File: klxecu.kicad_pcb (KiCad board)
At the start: 2 copper layers, 91 parts, among them IC1 SP721, J1 Conn_02x18_Top_Bottom, J2 ICSP, J3 Arduino Comms Header, Q1 STP62NS04Z, Q2 STP62NS04Z, Q3 IRF7301PBF, Q4 STP62NS04Z, U1 ATmega2560-16A, U2 MAX9924UAUB+, U3 ERZ-V14D220, U4 LM340T-5.0, U5 74LS02DR, U6 74LS14DR, U7 TC4422AVPA, Y1 16 mhz

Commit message: Updates
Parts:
- removed C25: u1, Capacitor_THT:C_Disc_D3.8mm_W2.6mm_P2.50mm
- removed C26: 47uf, Capacitor_THT:CP_Radial_Tantal_D6.0mm_P2.50mm
- removed C27: 1uf, Capacitor_SMD:C_0805_2012Metric_Pad1.18x1.45mm_HandSolder
- removed D2, D5, D7: 1N4004, Diode_THT:D_DO-41_SOD81_P10.16mm_Horizontal
- removed D6: 1N5919BG, Diode_THT:D_DO-41_SOD81_P7.62mm_Horizontal
- removed LED3, LED4: GREEN, LED_SMD:LED_0805_2012Metric_Pad1.15x1.40mm_HandSolder
- removed R34: 2k, Resistor_SMD:R_0805_2012Metric_Pad1.20x1.40mm_HandSolder
- removed R35: 47 2w, Resistor_THT:R_Axial_DIN0207_L6.3mm_D2.5mm_P5.08mm_Vertical
- removed U7: TC4422AVPA, Package_DIP:DIP-8_W7.62mm
- removed Y1: 16 mhz, Crystal:Resonator_SMD_Murata_CSTxExxV-3Pin_3.0x1.1mm_HandSoldering
- added A1: Pololu_Breakout_A4988, Module:Pololu_Breakout-16_15.2x20.3mm, F.Cu at (88.3, 146.1)
- added Q5: STP62NS04Z, Package_TO_SOT_THT:TO-220-3_Vertical, F.Cu at (153.0, 114.0)
- C10: value 1nf -> 0.1uf
- C12, C17: value 0.22uF -> 0.1uf
- C13: moved to B.Cu
- C14, C5, C7: value 0.1uf -> 0.22uF; moved to B.Cu
- C15: value 0.1uf -> 0.33uF; moved to B.Cu
- C16: value 0.1uf -> 10nf
- C18: value 0.22uF -> 1uf
- C19: value 0.33uF -> 100uf; footprint Capacitor_SMD:C_0805_2012Metric_Pad1.18x1.45mm_HandSolder -> Capacitor_THT:CP_Radial_D5.0mm_P2.50mm
- C2: value 0.1uf -> 1nf
- C20: value 10nf -> 1uf
- C21: value 0.1uf -> 10uf; footprint Capacitor_SMD:C_0805_2012Metric_Pad1.18x1.45mm_HandSolder -> Capacitor_THT:CP_Radial_Tantal_D6.0mm_P2.50mm
- C22: value 1uf -> u1; footprint Capacitor_SMD:C_0805_2012Metric_Pad1.18x1.45mm_HandSolder -> Capacitor_THT:C_Disc_D3.8mm_W2.6mm_P2.50mm
- C23: value 10uf -> u1; footprint Capacitor_THT:CP_Radial_Tantal_D6.0mm_P2.50mm -> Capacitor_THT:C_Disc_D3.8mm_W2.6mm_P2.50mm
- C24: value u1 -> 47uf; footprint Capacitor_THT:C_Disc_D3.8mm_W2.6mm_P2.50mm -> Capacitor_THT:CP_Radial_Tantal_D6.0mm_P2.50mm
- C4: value 22pf -> 0.1uf
- C6: value 0.1uf -> 0.22uF
- D1: value 1N5818 -> 1N4004; footprint Diode_THT:D_DO-41_SOD81_P7.62mm_Horizontal -> Diode_THT:D_DO-41_SOD81_P10.16mm_Horizontal
- D3: value 1N4004 -> 1N5818; footprint Diode_THT:D_DO-41_SOD81_P10.16mm_Horizontal -> Diode_THT:D_DO-41_SOD81_P7.62mm_Horizontal
- D4: value 1N4004 -> 1N5919BG; footprint Diode_THT:D_DO-41_SOD81_P10.16mm_Horizontal -> Diode_THT:D_DO-41_SOD81_P7.62mm_Horizontal
- J1: value Conn_02x18_Top_Bottom -> Conn_02x20_Odd_Even; footprint Connector_PinHeader_2.54mm:PinHeader_2x18_P2.54mm_Vertical -> Connector_PinSocket_2.54mm:PinSocket_2x20_P2.54mm_Vertical
- J2: value ICSP -> Conn_02x18_Top_Bottom; footprint Connector_PinHeader_2.54mm:PinHeader_2x03_P2.54mm_Vertical -> Connector_PinHeader_2.54mm:PinHeader_2x18_P2.54mm_Vertical
- J3: value Arduino Comms Header -> Conn_02x16_Odd_Even; footprint Connector_PinHeader_2.54mm:PinHeader_1x06_P2.54mm_Vertical -> Connector_PinSocket_2.54mm:PinSocket_2x16_P2.54mm_Vertical
- JP2: value Jumper_2_Open -> Jumper_3_Open; footprint Connector_PinHeader_2.54mm:PinHeader_1x02_P2.54mm_Vertical -> Connector_PinHeader_2.54mm:PinHeader_1x03_P2.54mm_Vertical
- Q3: value IRF7301PBF -> STP62NS04Z; footprint Package_SO:SOIC-8_3.9x4.9mm_P1.27mm -> Package_TO_SOT_THT:TO-220-3_Vertical
- R1: value 1M -> 10k; footprint Resistor_SMD:R_0805_2012Metric_Pad1.20x1.40mm_HandSolder -> Resistor_THT:R_Axial_DIN0207_L6.3mm_D2.5mm_P5.08mm_Vertical
- R10, R13, R14, R15, R9: value 470k -> 470; footprint Resistor_SMD:R_0805_2012Metric_Pad1.20x1.40mm_HandSolder -> Resistor_THT:R_Axial_DIN0207_L6.3mm_D2.5mm_P5.08mm_Vertical
- R11, R12, R16, R17, R19, R21, R25, R28: footprint Resistor_SMD:R_0805_2012Metric_Pad1.20x1.40mm_HandSolder -> Resistor_THT:R_Axial_DIN0207_L6.3mm_D2.5mm_P5.08mm_Vertical
- R18, R29: value 2k -> 100k; footprint Resistor_SMD:R_0805_2012Metric_Pad1.20x1.40mm_HandSolder -> Resistor_THT:R_Axial_DIN0207_L6.3mm_D2.5mm_P5.08mm_Vertical
- R2: value 10k -> 4.7k; footprint Resistor_SMD:R_0805_2012Metric_Pad1.20x1.40mm_HandSolder -> Resistor_THT:R_Axial_DIN0207_L6.3mm_D2.5mm_P5.08mm_Vertical
- R20, R30, R31: value 100k -> 1k; footprint Resistor_SMD:R_0805_2012Metric_Pad1.20x1.40mm_HandSolder -> Resistor_THT:R_Axial_DIN0207_L6.3mm_D2.5mm_P5.08mm_Vertical
- R22: value 1k -> 100k; footprint Resistor_SMD:R_0805_2012Metric_Pad1.20x1.40mm_HandSolder -> Resistor_THT:R_Axial_DIN0207_L6.3mm_D2.5mm_P5.08mm_Vertical
- R23, R24: value 10k -> 1k; footprint Resistor_SMD:R_0805_2012Metric_Pad1.20x1.40mm_HandSolder -> Resistor_THT:R_Axial_DIN0207_L6.3mm_D2.5mm_P5.08mm_Vertical
- R26, R27: value 1k -> 10k; footprint Resistor_SMD:R_0805_2012Metric_Pad1.20x1.40mm_HandSolder -> Resistor_THT:R_Axial_DIN0207_L6.3mm_D2.5mm_P5.08mm_Vertical
- R3: value 4.7k -> 2.49k; footprint Resistor_SMD:R_0805_2012Metric_Pad1.20x1.40mm_HandSolder -> Resistor_THT:R_Axial_DIN0207_L6.3mm_D2.5mm_P5.08mm_Vertical
- R32: value 1k -> 2k; footprint Resistor_SMD:R_0805_2012Metric_Pad1.20x1.40mm_HandSolder -> Resistor_THT:R_Axial_DIN0207_L6.3mm_D2.5mm_P5.08mm_Vertical
- R33: value 1k -> 47 2w; footprint Resistor_SMD:R_0805_2012Metric_Pad1.20x1.40mm_HandSolder -> Resistor_THT:R_Axial_DIN0207_L6.3mm_D2.5mm_P5.08mm_Vertical
- R4, R5: value 2.49k -> 10k; footprint Resistor_SMD:R_0805_2012Metric_Pad1.20x1.40mm_HandSolder -> Resistor_THT:R_Axial_DIN0207_L6.3mm_D2.5mm_P5.08mm_Vertical
- R6: value 10k -> 2.49k; footprint Resistor_SMD:R_0805_2012Metric_Pad1.20x1.40mm_HandSolder -> Resistor_THT:R_Axial_DIN0207_L6.3mm_D2.5mm_P5.08mm_Vertical
- R7: value 10k -> 470k; footprint Resistor_SMD:R_0805_2012Metric_Pad1.20x1.40mm_HandSolder -> Resistor_THT:R_Axial_DIN0207_L6.3mm_D2.5mm_P5.08mm_Vertical
- R8: value 470k -> 470
- U1: value ATmega2560-16A -> MAX9924UAUB+; footprint Package_QFP:TQFP-100_14x14mm_P0.5mm -> Package_SO:MSOP-10_3x3mm_P0.5mm
- U2: value MAX9924UAUB+ -> ATtiny84-20P; footprint Package_SO:MSOP-10_3x3mm_P0.5mm -> Package_DIP:DIP-14_W7.62mm
- U3: value ERZ-V14D220 -> 74LS14DR; footprint Varistor:RV_Disc_D7mm_W3.4mm_P5mm -> Package_SO:SOIC-14_3.9x8.7mm_P1.27mm
- U4: value LM340T-5.0 -> TC4422AVPA; footprint Package_TO_SOT_THT:TO-220-3_Vertical -> Package_DIP:DIP-8_W7.62mm
- U5: value 74LS02DR -> ERZ-V14D220; footprint Package_SO:SOIC-14_3.9x8.7mm_P1.27mm -> Varistor:RV_Disc_D7mm_W3.4mm_P5mm
- U6: value 74LS14DR -> LM340T-5.0; footprint Package_SO:SOIC-14_3.9x8.7mm_P1.27mm -> Package_TO_SOT_THT:TO-220-3_Vertical
- moved U6 201.0 mm to (245.1, 35.6), turned to -90 degrees
- moved U5 191.1 mm to (247.0, 25.4), turned to -90 degrees
- moved J2 186.8 mm to (25.4, 20.3)
- moved R26 184.4 mm to (51.0, 21.6)
- moved R1 184.4 mm to (33.7, 36.0), turned to 90 degrees
- moved R27 178.0 mm to (58.0, 24.1)
- moved JP1 172.6 mm to (33.7, 40.0)
- moved C22 168.3 mm to (229.2, 25.4), turned to -90 degrees
- moved R8 168.0 mm to (141.6, 17.1), turned to -90 degrees
- moved C13 162.6 mm to (134.6, 21.6), turned to 90 degrees
- moved R25 158.3 mm to (33.9, 117.5)
- moved R33 154.1 mm to (19.3, 114.9)
- moved R32 152.7 mm to (33.9, 125.7)
- moved R12 152.3 mm to (30.1, 184.2)
- moved C7 150.6 mm to (137.2, 31.8), turned to -90 degrees
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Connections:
- C1 pad 1: +5V -> TPS
- C10 pad 2: Net-(C10-Pad2) -> GND
- C11 pad 1: ARDUINO-A3 -> ATTINY-A1
- C12 pad 1: ARDUINO-A4 -> MAP
- C13 pad 1: ARDUINO-A5 -> ARDUINO-A2
- C14 pad 1: O2S + -> ARDUINO-A1
- C15 pad 1: Net-(C15-Pad1) -> ARDUINO-A0
- C16 pad 1: MAP -> +5V
- C17 pad 1: ARDUINO-A2 -> +5V
- C18 pad 1: ARDUINO-A1 -> +5V
- C19 pad 1: ARDUINO-A0 -> +BATT
- C2 pad 1: +5V -> Net-(C2-Pad1)
- C2 pad 2: GND -> Net-(C2-Pad2)
- C21 pad 1: +5V -> +12V
- C22 pad 1: +5V -> +12V
- C23 pad 1: +12V -> +5V
- C24 pad 1: +12V -> +5V
- C3 pad 1: +5V -> CLT
- C4 pad 1: ARDUINO-RST -> IAT
- C5 pad 1: Net-(C5-Pad1) -> ARDUINO-A3
- C6 pad 1: Net-(C6-Pad1) -> ARDUINO-A4
- C6 pad 2: ARDUINO-RST -> GND
- C7 pad 1: TPS -> ARDUINO-A5
- C8 pad 1: CLT -> SUB TPS
- C9 pad 1: IAT -> O2S +
- D1 pad 1: Net-(D1-Pad1) -> INJECTOR
- D1 pad 2: +12V -> Net-(D1-Pad2)
- D3 pad 1: FP RELAY -> Net-(D3-Pad1)
- D3 pad 2: Net-(D3-Pad2) -> +12V
- D4 pad 1: Net-(D4-Pad1) -> +5V
- D4 pad 2: ARDUINO-D6 -> GND
- IC1 pad 4: Earth -> GND
- J1 pad 1: +BATT -> unconnected-(J1-Pad1)
- J1 pad 10: TEMP WARN -> unconnected-(J1-Pad10)
- J1 pad 11: KICKSTAND SW -> unconnected-(J1-Pad11)
- J1 pad 12: AIR VALVE -> unconnected-(J1-Pad12)
- J1 pad 13: SUB A - -> ARDUINO-D4
- J1 pad 14: SUB B - -> ARDUINO-D5
- J1 pad 15: FAN RELAY -> ARDUINO-D6
- J1 pad 16: KILL SW -> ARDUINO-D7
- J1 pad 17: GND -> ARDUINO-D8
- J1 pad 18: GND -> ARDUINO-D8
- J1 pad 19: +12V -> unconnected-(J1-Pad19)
- J1 pad 2: NEUTRAL SW -> unconnected-(J1-Pad2)
- J1 pad 20: Vehicle Down -> unconnected-(J1-Pad20)
- J1 pad 21: CKP + -> unconnected-(J1-Pad21)
- J1 pad 23: TPS -> unconnected-(J1-Pad23)
- J1 pad 24: MAP -> unconnected-(J1-Pad24)
- J1 pad 25: O2S + -> unconnected-(J1-Pad25)
- J1 pad 26: GND -> unconnected-(J1-Pad26)
- J1 pad 27: CKP - -> unconnected-(J1-Pad27)
- J1 pad 28: GND -> ARDUINO-D19
- J1 pad 29: FP RELAY -> unconnected-(J1-Pad29)
- J1 pad 3: CHECK ENGINE -> GND
- J1 pad 30: CLUTCH SW -> unconnected-(J1-Pad30)
- J1 pad 31: +5V -> unconnected-(J1-Pad31)
- J1 pad 32: SUB B + -> ARDUINO-D23
- J1 pad 33: SUB A + -> unconnected-(J1-Pad33)
- J1 pad 34: INJECTOR -> unconnected-(J1-Pad34)
- J1 pad 35: O2S HEAT + -> unconnected-(J1-Pad35)
- J1 pad 36: IGN -> unconnected-(J1-Pad36)
- J1 pad 4: CLT -> GND
- J1 pad 5: ARDUINO-D3 -> +5V
- J1 pad 6: GND -> +5V
- J1 pad 7: IAT -> unconnected-(J1-Pad7)
- J1 pad 8: SPEED -> ARDUINO-RST
- J1 pad 9: SUB TPS -> unconnected-(J1-Pad9)
- J2 pad 1: Net-(J2-Pad1) -> +BATT
- J2 pad 2: +5V -> NEUTRAL SW
- J2 pad 3: Net-(J2-Pad3) -> CHECK ENGINE
- J2 pad 4: Net-(J2-Pad4) -> CLT
- J2 pad 5: ARDUINO-RST -> ARDUINO-D3
- J3 pad 1: GND -> ARDUINO-A0
- J3 pad 2: GND -> ARDUINO-A1
- J3 pad 3: +5V -> ARDUINO-A2
- J3 pad 4: Net-(J3-Pad4) -> ARDUINO-A3
- J3 pad 5: Net-(J3-Pad5) -> ARDUINO-A4
- J3 pad 6: Net-(C6-Pad1) -> ARDUINO-A5
- JP2 pad 1: Net-(D5-Pad1) -> +5V
- JP2 pad 2: Net-(D4-Pad1) -> Net-(A1-Pad8)
- LED1 pad 1: Net-(D2-Pad2) -> Net-(D1-Pad2)
- LED2 pad 1: Net-(D3-Pad2) -> GND
- Q3 pad 1: GND -> Net-(Q3-Pad1)
- Q3 pad 2: Net-(Q3-Pad2) -> CHECK ENGINE
- Q4 pad 2: FAN RELAY -> TEMP WARN
- R1 pad 1: Net-(R1-Pad1) -> +5V
- R1 pad 2: Net-(R1-Pad2) -> ARDUINO-D3
- R10 pad 1: IAT -> SUB TPS
- R10 pad 2: ARDUINO-A5 -> ATTINY-A1
- R11 pad 1: Net-(C15-Pad1) -> Net-(C10-Pad1)
- R12 pad 2: Net-(C15-Pad1) -> Net-(C10-Pad1)
- R14 pad 1: Net-(C15-Pad1) -> Net-(C10-Pad1)
- R18 pad 1: KILL SW -> ARDUINO-D8
- R18 pad 2: Net-(LED2-Pad2) -> GND
- R19 pad 1: ARDUINO-D8 -> ARDUINO-D4
- R2 pad 1: +5V -> CKP+
- R2 pad 2: ARDUINO-D3 -> CKP-
- R20 pad 1: ARDUINO-D4 -> Net-(Q1-Pad1)
- R20 pad 2: GND -> ARDUINO-D8
- R21 pad 1: Net-(Q1-Pad1) -> Net-(Q2-Pad1)
- R21 pad 2: ARDUINO-D8 -> ARDUINO-D4
- R22 pad 1: Net-(Q2-Pad1) -> ATTINY-D10
- R22 pad 2: ARDUINO-D4 -> GND
- R23 pad 1: +5V -> Net-(Q3-Pad1)
- R23 pad 2: NEUTRAL SW -> ATTINY-D10
- R24 pad 1: +5V -> ARDUINO-D23
- R24 pad 2: KICKSTAND SW -> Net-(R24-Pad2)
- R25 pad 1: Net-(D4-Pad1) -> Net-(R24-Pad2)
- R26 pad 1: Net-(Q3-Pad4) -> +5V
- R26 pad 2: Net-(D4-Pad1) -> NEUTRAL SW
- R27 pad 1: ARDUINO-D23 -> +5V
- R27 pad 2: Net-(R27-Pad2) -> KICKSTAND SW
- R28 pad 1: Net-(R27-Pad2) -> ARDUINO-D5
- R29 pad 1: +12V -> ARDUINO-D7
- R29 pad 2: Net-(LED3-Pad2) -> GND
- R3 pad 1: CKP+ -> +5V
- R3 pad 2: CKP- -> CLT
- R30 pad 1: ARDUINO-D5 -> Net-(Q5-Pad1)
- R30 pad 2: GND -> ARDUINO-D5
- R31 pad 1: ARDUINO-D7 -> Net-(Q4-Pad1)
- R31 pad 2: GND -> ARDUINO-D7
- R32 pad 1: Net-(Q4-Pad1) -> Net-(R32-Pad1)
- R32 pad 2: ARDUINO-D5 -> Net-(LED2-Pad2)
- R33 pad 1: Net-(Q3-Pad2) -> IGN
- R33 pad 2: ARDUINO-D7 -> Net-(R32-Pad1)
- R4 pad 1: +5V -> Net-(C2-Pad1)
- R4 pad 2: CLT -> CKP+
- R5 pad 1: +5V -> CKP-
- R5 pad 2: IAT -> Net-(C2-Pad2)
- R6 pad 1: Net-(C10-Pad1) -> +5V
- R6 pad 2: CKP+ -> IAT
- R7 pad 1: CKP- -> TPS
- R7 pad 2: Net-(C10-Pad2) -> ARDUINO-A3
- R8 pad 1: TPS -> CLT
- R8 pad 2: ARDUINO-A3 -> ARDUINO-A4
- R9 pad 1: CLT -> IAT
- R9 pad 2: ARDUINO-A4 -> ARDUINO-A5
- U1 pad 1: ARDUINO-D4 -> Net-(C2-Pad1)
- U1 pad 2: Net-(J3-Pad4) -> Net-(C2-Pad2)
- U1 pad 3: Net-(J3-Pad5) -> unconnected-(U1-Pad3)
- U1 pad 4: unconnected-(U1-Pad4) -> GND
- U1 pad 5: ARDUINO-D5 -> GND
- U1 pad 6: unconnected-(U1-Pad6) -> GND
- U1 pad 7: ARDUINO-D3 -> ARDUINO-D19
- U1 pad 9: unconnected-(U1-Pad9) -> GND
- U2 pad 1: Net-(C10-Pad1) -> +5V
- U2 pad 10: +5V -> ATTINY-A3
- U2 pad 2: Net-(C10-Pad2) -> ATTINY-D10
- U2 pad 3: unconnected-(U2-Pad3) -> ARDUINO-RST
- U2 pad 4: GND -> +5V
- U2 pad 5: GND -> ARDUINO-D6
- U2 pad 6: GND -> unconnected-(U2-Pad6)
- U2 pad 7: ARDUINO-D19 -> Net-(A1-Pad16)
- U2 pad 8: unconnected-(U2-Pad8) -> Net-(A1-Pad15)
- U2 pad 9: GND -> ATTINY-A4
- U3 pad 1: +12V -> Vehicle Down
- U3 pad 2: GND -> ATTINY-A2
- U4 pad 1: Net-(D1-Pad1) -> +5V
- U4 pad 2: GND -> Net-(R24-Pad2)
- U4 pad 3: +5V -> unconnected-(U4-Pad3)
- U5 pad 1: ARDUINO-RST -> +12V
- U5 pad 2: Net-(U5-Pad2) -> GND
- U6 pad 1: Vehicle Down -> Net-(D3-Pad1)
- U6 pad 2: Net-(U5-Pad2) -> GND
- U6 pad 3: NEUTRAL SW -> +5V
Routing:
- net +12V: track 95.2 -> 29.5 mm
- net Net-(D1-Pad1): track 16.0 -> 0.00 mm
- net ARDUINO-RST: track 14.5 -> 0.00 mm
- net Net-(U5-Pad2): track 12.0 -> 0.00 mm
- net Net-(U5-Pad5): track 12.0 -> 0.00 mm
- net Net-(U5-Pad6): track 11.9 -> 0.00 mm
- net KICKSTAND SW: track 9.65 -> 0.00 mm
- net ARDUINO-D19: track 0.00 -> 9.41 mm
- net GND: track 58.5 -> 67.0 mm
- net Net-(U5-Pad11): track 7.95 -> 0.00 mm
- net Net-(C2-Pad1): track 0.00 -> 6.28 mm
- net Net-(C2-Pad2): track 0.00 -> 5.67 mm
- net Net-(U5-Pad13): track 5.48 -> 0.00 mm
- net Net-(D3-Pad1): track 0.00 -> 5.10 mm
- net NEUTRAL SW: track 4.79 -> 0.00 mm
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
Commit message: more updates
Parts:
- C13, C14, C15, C5, C7: moved to F.Cu
- R1, R10, R11, R12, R13, R14, R15, R16, R17, R18, R19, R2, R20, R21, R22, R23, R24, R25, R26, R27, R28, R29, R3, R30, R31, R32, R6, R9: footprint Resistor_THT:R_Axial_DIN0207_L6.3mm_D2.5mm_P5.08mm_Vertical -> Resistor_SMD:R_0805_2012Metric_Pad1.20x1.40mm_HandSolder
- R4, R5: footprint Resistor_THT:R_Axial_DIN0207_L6.3mm_D2.5mm_P5.08mm_Vertical -> Resistor_SMD:R_0805_2012Metric
- R7: value 470k -> 470; footprint Resistor_THT:R_Axial_DIN0207_L6.3mm_D2.5mm_P5.08mm_Vertical -> Resistor_SMD:R_0805_2012Metric_Pad1.20x1.40mm_HandSolder
- moved C8 182.8 mm to (88.9, 142.7)
- moved R10 180.6 mm to (85.1, 141.5), turned to 90 degrees
- moved C11 177.3 mm to (88.9, 140.2)
- moved R9 174.3 mm to (118.2, 32.0), turned to 90 degrees
- moved R12 168.8 mm to (104.0, 32.4), turned to 90 degrees
- moved C4 168.2 mm to (121.4, 33.9)
- moved R13 165.3 mm to (111.7, 21.5), turned to -90 degrees
- moved R6 163.8 mm to (121.4, 36.5), turned to 180 degrees
- moved C9 163.0 mm to (114.8, 20.0)
- moved R11 162.9 mm to (102.8, 29.5), turned to 180 degrees
- moved C10 162.5 mm to (106.6, 32.4), turned to -90 degrees
- moved R14 155.8 mm to (107.2, 29.5)
- moved U1 106.8 mm to (129.2, 54.5)
- moved C16 106.5 mm to (139.0, 54.5)
- moved C17 106.5 mm to (136.4, 54.5)
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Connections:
- A1 pad 8: Net-(A1-Pad8) -> Net-(C19-Pad1)
- C19 pad 1: +BATT -> Net-(C19-Pad1)
- J1 pad 12: unconnected-(J1-Pad12) -> ARDUINO-D3
- J1 pad 18: ARDUINO-D8 -> unconnected-(J1-Pad18)
- JP2 pad 2: Net-(A1-Pad8) -> Net-(C19-Pad1)
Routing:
- net +5V: track 36.4 -> 112.5 mm
- net GND: track 67.0 -> 122.7 mm
- net ARDUINO-A2: track 2.84 -> 37.4 mm
- net ARDUINO-A0: track 2.84 -> 33.2 mm
- net ARDUINO-A1: track 2.70 -> 32.7 mm
- net ARDUINO-A5: track 2.70 -> 29.7 mm
- net ARDUINO-A3: track 2.70 -> 22.8 mm
- net ARDUINO-A4: track 0.00 -> 19.3 mm
- net ATTINY-A4: track 0.00 -> 18.5 mm
- net ATTINY-A2: track 0.00 -> 18.5 mm
- net ATTINY-A3: track 0.00 -> 18.5 mm
- net Net-(A1-Pad15): track 0.00 -> 17.6 mm
- net Net-(A1-Pad16): track 0.00 -> 11.6 mm
- net Net-(R24-Pad2): track 0.00 -> 11.4 mm
- net ATTINY-D10: track 4.00 -> 15.3 mm
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
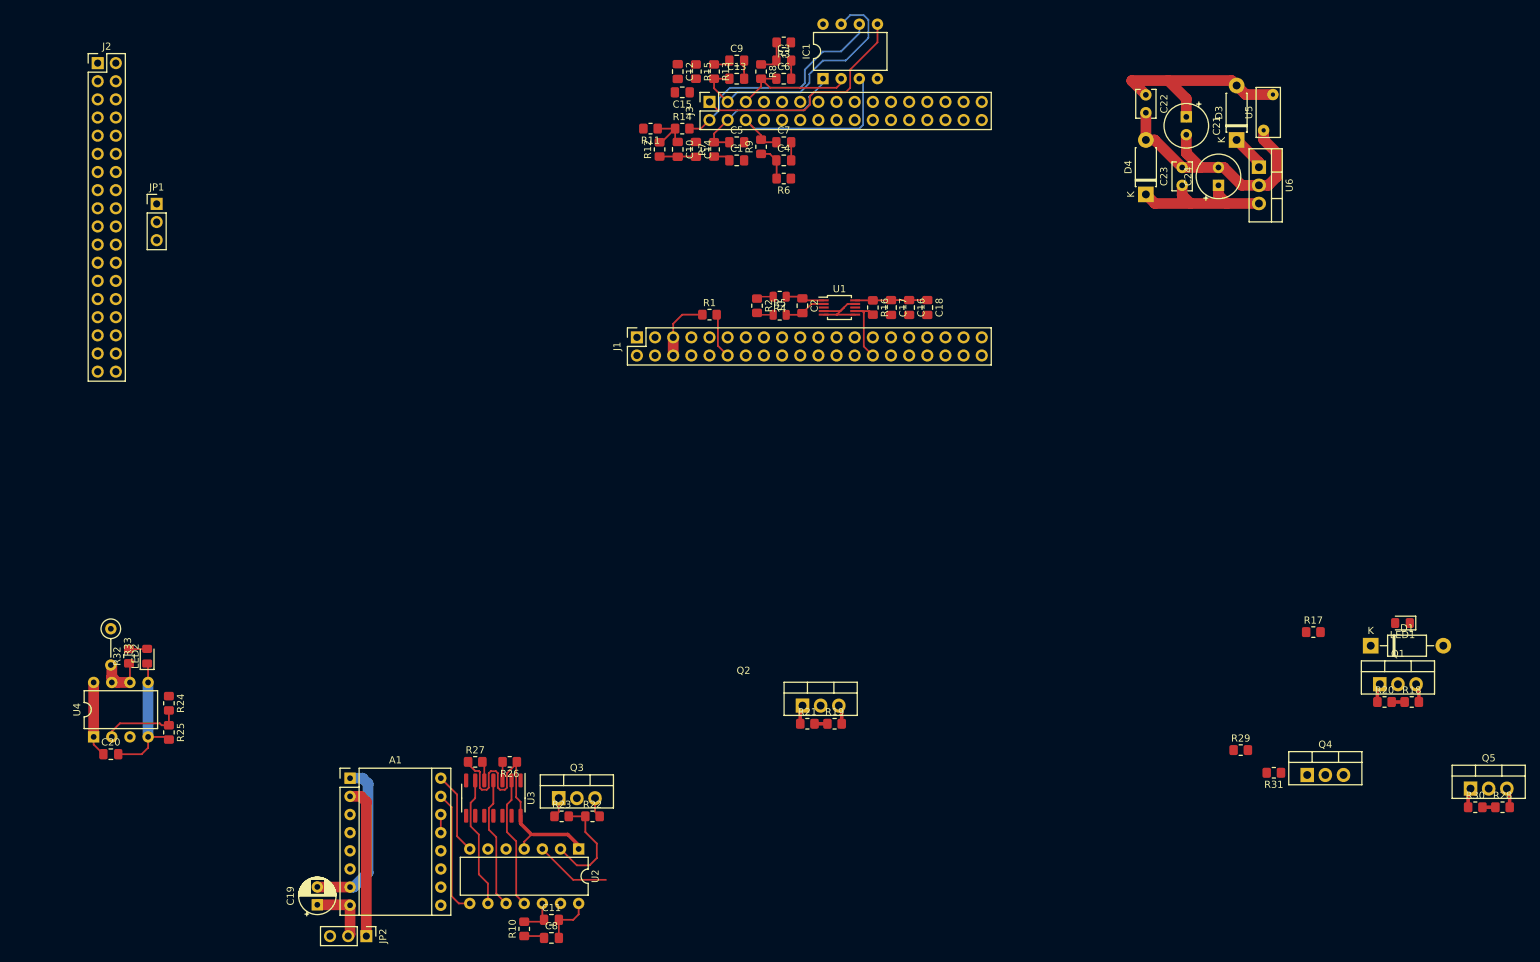
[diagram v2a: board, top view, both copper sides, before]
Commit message: Technically all the nets are connected
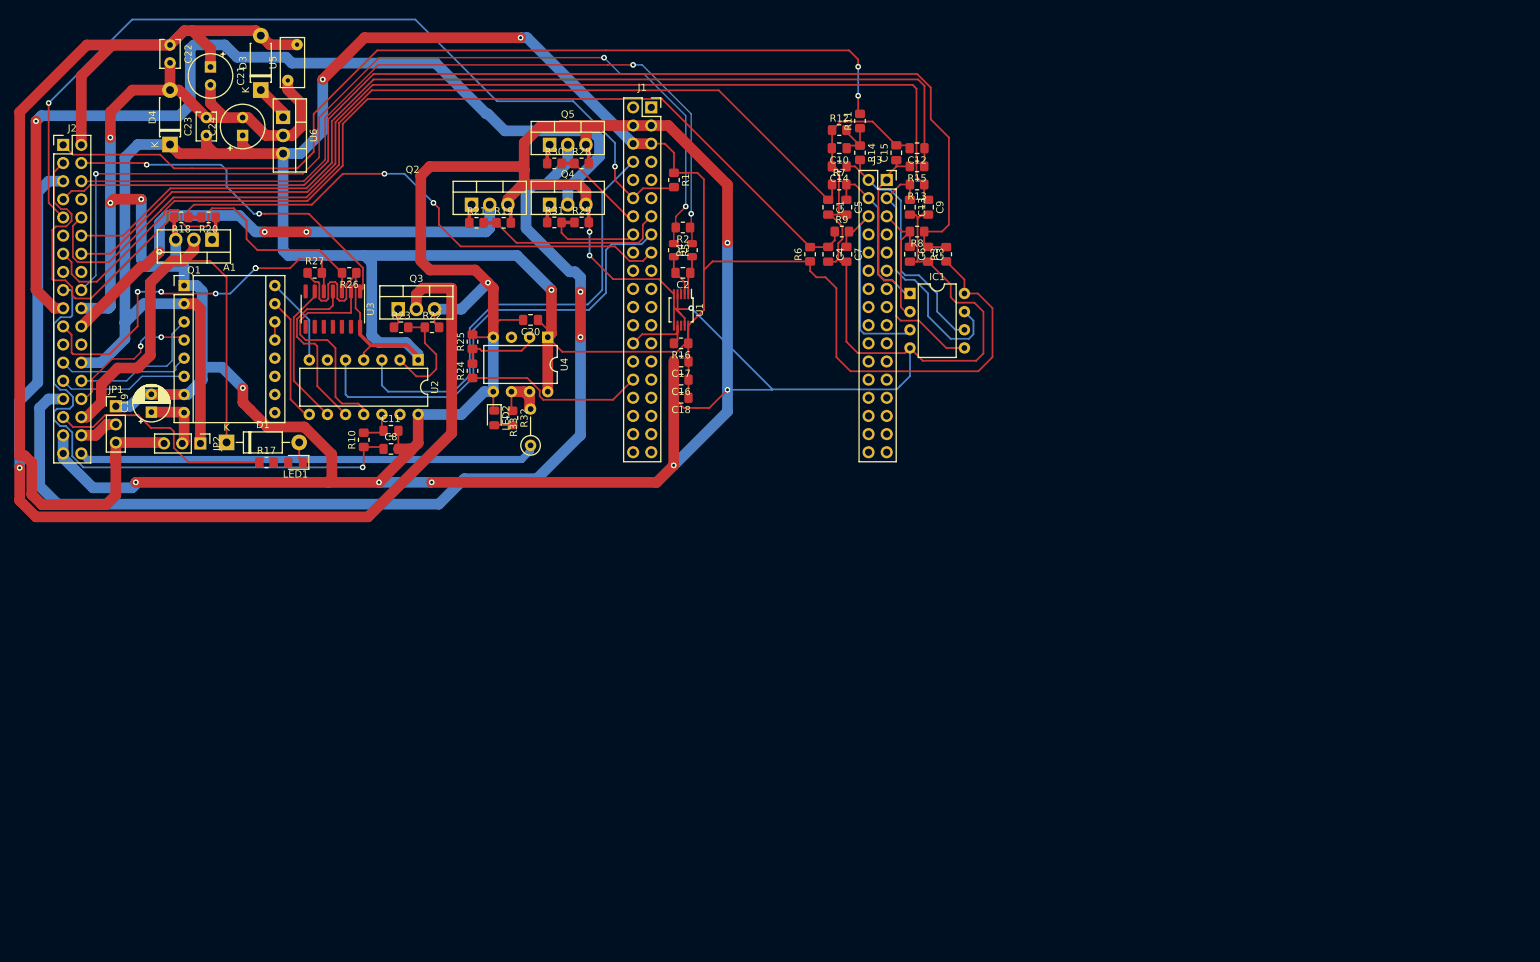
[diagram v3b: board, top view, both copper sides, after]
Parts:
- moved R18 185.1 mm to (37.1, 41.9), turned to 180 degrees
- moved R20 178.0 mm to (40.9, 41.9), turned to 180 degrees
- moved Q1 174.9 mm to (41.4, 45.0), turned to 180 degrees
- moved D1 162.6 mm to (43.4, 73.4)
- moved Q5 157.2 mm to (88.6, 31.8)
- moved R28 157.2 mm to (93.1, 34.4)
- moved R30 157.2 mm to (89.3, 34.4)
- moved LED1 156.5 mm to (53.1, 76.2)
- moved R17 148.4 mm to (49.0, 76.2)
- moved C21 136.7 mm to (41.2, 20.9)
- moved C22 136.7 mm to (35.5, 17.8)
- moved C24 136.7 mm to (45.7, 30.4)
- moved D3 136.7 mm to (48.2, 24.1)
- moved D4 136.7 mm to (35.5, 31.7)
- moved U5 136.7 mm to (53.3, 17.7)
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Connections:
- JP2 pad 3: +BATT -> +12V
- R2 pad 1: CKP+ -> CKP +
- R2 pad 2: CKP- -> CKP -
- R4 pad 2: CKP+ -> CKP +
- R5 pad 1: CKP- -> CKP -
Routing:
- net GND: track 122.7 -> 680.1 mm, vias 0 -> 14
- net +5V: track 112.5 -> 429.0 mm, vias 0 -> 3
- net CLT: track 4.92 -> 161.9 mm
- net O2S +: track 2.36 -> 146.5 mm
- net FAN RELAY: track 0.00 -> 143.2 mm, vias 0 -> 2
- net CHECK ENGINE: track 0.00 -> 142.3 mm, vias 0 -> 1
- net MAP: track 0.00 -> 142.1 mm
- net TEMP WARN: track 0.00 -> 132.9 mm, vias 0 -> 1
- net CKP -: track 0.00 -> 132.0 mm, vias 0 -> 3
- net TPS: track 2.36 -> 134.2 mm
- net +BATT: track 0.00 -> 130.8 mm, vias 0 -> 2
- net IAT: track 5.07 -> 135.0 mm
- net +12V: track 29.5 -> 157.3 mm
- net ARDUINO-D3: track 6.35 -> 123.2 mm, vias 0 -> 2
- net CKP +: track 0.00 -> 116.7 mm, vias 0 -> 2
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
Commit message: Misc updates
- Add pin to handle cluch for launch control
- re-do PCB from scratch (more things go on the backside this time)
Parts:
- removed D3: 1N5818, Diode_THT:D_DO-41_SOD81_P7.62mm_Horizontal
- removed D4: 1N5919BG, Diode_THT:D_DO-41_SOD81_P7.62mm_Horizontal
- removed JP2: Jumper_3_Open, Connector_PinHeader_2.54mm:PinHeader_1x03_P2.54mm_Vertical
- removed LED1, LED2: GREEN, LED_SMD:LED_0805_2012Metric_Pad1.15x1.40mm_HandSolder
- removed R16, R20, R21, R23, R24, R30, R31: 1k, Resistor_SMD:R_0805_2012Metric_Pad1.20x1.40mm_HandSolder
- removed R17, R32: 2k, Resistor_SMD:R_0805_2012Metric_Pad1.20x1.40mm_HandSolder
- removed R18, R19, R22, R25, R28, R29: 100k, Resistor_SMD:R_0805_2012Metric_Pad1.20x1.40mm_HandSolder
- removed R26, R27: 10k, Resistor_SMD:R_0805_2012Metric_Pad1.20x1.40mm_HandSolder
- removed R33: 47 2w, Resistor_THT:R_Axial_DIN0207_L6.3mm_D2.5mm_P5.08mm_Vertical
- added D2: 1N5919BG, Diode_THT:D_DO-41_SOD81_P7.62mm_Horizontal, F.Cu at (54.0, 27.3)
- added J4: Conn_01x01_Male, Connector_PinHeader_2.54mm:PinHeader_1x01_P2.54mm_Vertical, F.Cu at (248.2, 86.7)
- added Q6: STP62NS04Z, Package_TO_SOT_THT:TO-220-3_Vertical, F.Cu at (237.7, 79.3)
- added Q7: STP62NS04Z, Package_TO_SOT_THT:TO-220-3_Vertical, F.Cu at (77.5, 117.2)
- added RN1: 470, Resistor_THT:R_Array_SIP12, F.Cu at (116.8, 25.4)
- added RN2: 100k, Resistor_THT:R_Array_SIP6, F.Cu at (62.2, 151.8)
- added RN3: 1k, Resistor_THT:R_Array_SIP12, F.Cu at (55.9, 143.5)
- added RN4: 10k, Resistor_THT:R_Array_SIP4, F.Cu at (94.6, 54.6)
- C1: value 0.1uf -> 10uf; footprint Capacitor_SMD:C_0805_2012Metric_Pad1.18x1.45mm_HandSolder -> Capacitor_THT:CP_Radial_Tantal_D6.0mm_P2.50mm
- C10: value 0.1uf -> 0.22uF; moved to B.Cu
- C12: value 0.1uf -> 0.22uF
- C14, C7: value 0.22uF -> 0.1uf
- C15: value 0.33uF -> 0.1uf
- C16: value 10nf -> 0.1uf
- C17: value 0.1uf -> 0.33uF
- C18: value 1uf -> 0.22uF
- C19: value 100uf -> 0.22uF; footprint Capacitor_THT:CP_Radial_D5.0mm_P2.50mm -> Capacitor_SMD:C_0805_2012Metric_Pad1.18x1.45mm_HandSolder
- C2: value 1nf -> u1; footprint Capacitor_SMD:C_0805_2012Metric_Pad1.18x1.45mm_HandSolder -> Capacitor_THT:C_Disc_D3.8mm_W2.6mm_P2.50mm
- C20: value 1uf -> 10nf; moved to B.Cu
- C21: value 10uf -> 0.1uf; footprint Capacitor_THT:CP_Radial_Tantal_D6.0mm_P2.50mm -> Capacitor_SMD:C_0805_2012Metric_Pad1.18x1.45mm_HandSolder; moved to B.Cu
- C22: value u1 -> 1uf; footprint Capacitor_THT:C_Disc_D3.8mm_W2.6mm_P2.50mm -> Capacitor_SMD:C_0805_2012Metric_Pad1.18x1.45mm_HandSolder; moved to B.Cu
- C23: value u1 -> 100uf; footprint Capacitor_THT:C_Disc_D3.8mm_W2.6mm_P2.50mm -> Capacitor_THT:CP_Radial_D5.0mm_P2.50mm
- C24: value 47uf -> 1uf; footprint Capacitor_THT:CP_Radial_Tantal_D6.0mm_P2.50mm -> Capacitor_SMD:C_0805_2012Metric_Pad1.18x1.45mm_HandSolder
- C3: value 0.1uf -> u1; footprint Capacitor_SMD:C_0805_2012Metric_Pad1.18x1.45mm_HandSolder -> Capacitor_THT:C_Disc_D3.8mm_W2.6mm_P2.50mm
- C4: value 0.1uf -> 47uf; footprint Capacitor_SMD:C_0805_2012Metric_Pad1.18x1.45mm_HandSolder -> Capacitor_THT:CP_Radial_Tantal_D6.0mm_P2.50mm
- C5: value 0.22uF -> 0.1uf; moved to B.Cu
- C6: value 0.22uF -> 1nf; moved to B.Cu
- D1: value 1N4004 -> 1N5818; footprint Diode_THT:D_DO-41_SOD81_P10.16mm_Horizontal -> Diode_THT:D_DO-41_SOD81_P7.62mm_Horizontal
- J2: value Conn_02x18_Top_Bottom -> Conn_02x18_Odd_Even
- JP1: value O2 HEAT ENABLE -> Jumper_3_Open
- Q1: value STP62NS04Z -> 2N3904; footprint Package_TO_SOT_THT:TO-220-3_Vertical -> Package_TO_SOT_THT:TO-92_Inline
- R1: value 10k -> 4.7k; moved to B.Cu
- R10: value 470 -> 10k; footprint Resistor_SMD:R_0805_2012Metric_Pad1.20x1.40mm_HandSolder -> Resistor_SMD:R_0805_2012Metric
- R11: value 3.9k -> 1k
- R13: value 470 -> 100k
- R14: value 470 -> 47 2w; footprint Resistor_SMD:R_0805_2012Metric_Pad1.20x1.40mm_HandSolder -> Resistor_THT:R_Axial_DIN0207_L6.3mm_D2.5mm_P5.08mm_Vertical
- R15, R7, R9: value 470 -> 1k
- R2: value 4.7k -> 10k; footprint Resistor_SMD:R_0805_2012Metric_Pad1.20x1.40mm_HandSolder -> Resistor_SMD:R_0805_2012Metric; moved to B.Cu
- R3: value 2.49k -> 10k; footprint Resistor_SMD:R_0805_2012Metric_Pad1.20x1.40mm_HandSolder -> Resistor_SMD:R_0805_2012Metric; moved to B.Cu
- R4: value 10k -> 2.49k; footprint Resistor_SMD:R_0805_2012Metric -> Resistor_SMD:R_0805_2012Metric_Pad1.20x1.40mm_HandSolder
- R5: value 10k -> 470; footprint Resistor_SMD:R_0805_2012Metric -> Resistor_SMD:R_0805_2012Metric_Pad1.20x1.40mm_HandSolder; moved to B.Cu
- R6: value 2.49k -> 3.9k
- R8: value 470 -> 2.49k
- U1: value MAX9924UAUB+ -> ERZ-V14D220; footprint Package_SO:MSOP-10_3x3mm_P0.5mm -> Varistor:RV_Disc_D7mm_W3.4mm_P5mm
- U2: value ATtiny84-20P -> LM340T-5.0; footprint Package_DIP:DIP-14_W7.62mm -> Package_TO_SOT_THT:TO-220-3_Vertical
- U3: value 74LS14DR -> MAX9924UAUB+; footprint Package_SO:SOIC-14_3.9x8.7mm_P1.27mm -> Package_SO:MSOP-10_3x3mm_P0.5mm; moved to B.Cu
- U4: value TC4422AVPA -> ATtiny84-20P; footprint Package_DIP:DIP-8_W7.62mm -> Package_DIP:DIP-14_W7.62mm
- U5: value ERZ-V14D220 -> 74LS14DR; footprint Varistor:RV_Disc_D7mm_W3.4mm_P5mm -> Package_SO:SOIC-14_3.9x8.7mm_P1.27mm; moved to B.Cu
- U6: value LM340T-5.0 -> TC4422AVPA; footprint Package_TO_SOT_THT:TO-220-3_Vertical -> Package_DIP:DIP-8_W7.62mm
- moved Q1 188.8 mm to (221.9, 100.5), turned to 0 degrees
- moved C24 179.6 mm to (204.0, 115.3), turned to 0 degrees
- moved C19 177.1 mm to (198.6, 131.9), turned to 0 degrees
- moved JP1 171.6 mm to (191.8, 119.2)
- moved C8 171.1 mm to (236.8, 89.4)
- moved R10 168.5 mm to (227.8, 105.9), turned to 0 degrees
- moved C11 160.8 mm to (223.2, 107.6)
- moved R12 130.4 mm to (248.3, 82.9)
- moved R11 126.8 mm to (241.6, 92.4), turned to 0 degrees
- moved C7 126.6 mm to (253.2, 76.9), turned to 0 degrees
- moved R7 122.3 mm to (236.8, 95.4)
- moved R4 121.5 mm to (210.7, 112.3), turned to 0 degrees
- moved C17 121.5 mm to (218.4, 110.6), turned to 0 degrees
- moved C15 119.6 mm to (248.4, 76.9), turned to 0 degrees
- moved R9 118.4 mm to (234.4, 98.8)
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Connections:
- A1 pad 8: Net-(C19-Pad1) -> Net-(A1-Pad8)
- C1 pad 1: TPS -> +12V
- C10 pad 1: Net-(C10-Pad1) -> ATTINY-A1
- C11 pad 1: ATTINY-A1 -> ARDUINO-A5
- C12 pad 1: MAP -> ARDUINO-A3
- C13 pad 1: ARDUINO-A2 -> ARDUINO-A1
- C14 pad 1: ARDUINO-A1 -> MAP
- C15 pad 1: ARDUINO-A0 -> CLT
- C16 pad 1: +5V -> O2S +
- C17 pad 1: +5V -> ARDUINO-A0
- C18 pad 1: +5V -> ARDUINO-A4
- C19 pad 1: Net-(C19-Pad1) -> ARDUINO-A2
- C2 pad 1: Net-(C2-Pad1) -> +12V
- C2 pad 2: Net-(C2-Pad2) -> GND
- C21 pad 1: +12V -> +5V
- C22 pad 1: +12V -> +5V
- C23 pad 1: +5V -> Net-(A1-Pad8)
- C3 pad 1: CLT -> +5V
- C4 pad 1: IAT -> +5V
- C5 pad 1: ARDUINO-A3 -> SUB TPS
- C6 pad 1: ARDUINO-A4 -> Net-(C6-Pad1)
- C6 pad 2: GND -> Net-(C6-Pad2)
- C7 pad 1: ARDUINO-A5 -> IAT
- C8 pad 1: SUB TPS -> TPS
- C9 pad 1: O2S + -> Net-(C9-Pad1)
- D1 pad 1: INJECTOR -> Net-(D1-Pad1)
- D1 pad 2: Net-(D1-Pad2) -> +12V
- IC1 pad 1: ARDUINO-A3 -> ARDUINO-A0
- IC1 pad 2: ARDUINO-A4 -> ARDUINO-A2
- IC1 pad 3: ARDUINO-A5 -> ARDUINO-A4
- IC1 pad 5: ARDUINO-A0 -> ARDUINO-A1
- IC1 pad 6: ARDUINO-A1 -> ARDUINO-A5
- IC1 pad 7: ARDUINO-A2 -> ARDUINO-A3
- J1 pad 12: ARDUINO-D3 -> unconnected-(J1-Pad12)
- J1 pad 14: ARDUINO-D5 -> unconnected-(J1-Pad14)
- J1 pad 15: ARDUINO-D6 -> unconnected-(J1-Pad15)
- J1 pad 16: ARDUINO-D7 -> unconnected-(J1-Pad16)
- J1 pad 19: unconnected-(J1-Pad19) -> Net-(J1-Pad19)
- J1 pad 39: unconnected-(J1-Pad39) -> ARDUINO-D30
- J2 pad 10: TEMP WARN -> TPS
- J2 pad 11: KICKSTAND SW -> GND
- J2 pad 12: AIR VALVE -> MAP
- J2 pad 13: SUB A - -> IAT
- J2 pad 14: SUB B - -> O2S +
- J2 pad 15: FAN RELAY -> SPEED
- J2 pad 16: KILL SW -> GND
- J2 pad 17: GND -> SUB TPS
- J2 pad 18: GND -> CKP -
- J2 pad 19: +12V -> TEMP WARN
- J2 pad 2: NEUTRAL SW -> +12V
- J2 pad 20: Vehicle Down -> GND
- J2 pad 21: CKP + -> KICKSTAND SW
- J2 pad 22: unconnected-(J2-Pad22) -> FP RELAY
- J2 pad 23: TPS -> AIR VALVE
- J2 pad 24: MAP -> CLUTCH SW
- J2 pad 25: O2S + -> SUB A -
- J2 pad 26: GND -> +5V
- J2 pad 27: CKP - -> SUB B -
- J2 pad 28: GND -> SUB B +
- J2 pad 29: FP RELAY -> FAN RELAY
- J2 pad 3: CHECK ENGINE -> NEUTRAL SW
- J2 pad 30: CLUTCH SW -> SUB A +
- J2 pad 31: +5V -> KILL SW
- J2 pad 32: SUB B + -> INJECTOR
- J2 pad 33: SUB A + -> GND
- J2 pad 34: INJECTOR -> O2S HEAT +
- J2 pad 35: O2S HEAT + -> GND
- J2 pad 4: CLT -> Vehicle Down
- J2 pad 5: ARDUINO-D3 -> CHECK ENGINE
- J2 pad 6: GND -> CKP +
- J2 pad 7: IAT -> CLT
- J2 pad 8: SPEED -> unconnected-(J2-Pad8)
- J2 pad 9: SUB TPS -> SELF DIAG
- J3 pad 17: unconnected-(J3-Pad17) -> ARDUINO-D32
- J3 pad 19: unconnected-(J3-Pad19) -> ARDUINO-D34
- J3 pad 23: unconnected-(J3-Pad23) -> ARDUINO-D38
- J3 pad 27: unconnected-(J3-Pad27) -> ARDUINO-D42
- JP1 pad 1: GND -> +5V
- JP1 pad 2: O2S HEAT + -> Net-(A1-Pad8)
- Q1 pad 1: Net-(Q1-Pad1) -> GND
- Q1 pad 2: INJECTOR -> Net-(Q1-Pad2)
- Q1 pad 3: GND -> Net-(J4-Pad1)
- Q2 pad 2: FP RELAY -> INJECTOR
- Q3 pad 2: CHECK ENGINE -> FP RELAY
- Q4 pad 2: TEMP WARN -> FAN RELAY
- Q5 pad 2: FAN RELAY -> CHECK ENGINE
- R1 pad 1: +5V -> CKP +
- R1 pad 2: ARDUINO-D3 -> CKP -
- R10 pad 1: SUB TPS -> Net-(J4-Pad1)
- R10 pad 2: ATTINY-A1 -> +12V
- R11 pad 1: Net-(C10-Pad1) -> +5V
- R11 pad 2: +BATT -> ARDUINO-D19
- R12 pad 1: GND -> ARDUINO-D23
- R12 pad 2: Net-(C10-Pad1) -> Net-(R12-Pad2)
- R13 pad 1: O2S + -> Net-(R12-Pad2)
- R13 pad 2: ARDUINO-A2 -> GND
- R14 pad 1: Net-(C10-Pad1) -> IGN
- R14 pad 2: ARDUINO-A1 -> Net-(R14-Pad2)
- R15 pad 1: MAP -> Net-(J1-Pad19)
- R15 pad 2: ARDUINO-A0 -> CLUTCH SW
- R2 pad 1: CKP + -> Net-(C6-Pad1)
- R2 pad 2: CKP - -> CKP +
- R3 pad 1: +5V -> CKP -
- R3 pad 2: CLT -> Net-(C6-Pad2)
- R4 pad 1: Net-(C2-Pad1) -> +5V
- R4 pad 2: CKP + -> IAT
- R5 pad 1: CKP - -> SUB TPS
- R5 pad 2: Net-(C2-Pad2) -> ATTINY-A1
- R6 pad 1: +5V -> Net-(C9-Pad1)
- R6 pad 2: IAT -> +12V
- R7 pad 1: TPS -> GND
- R7 pad 2: ARDUINO-A3 -> Net-(C9-Pad1)
- R8 pad 1: CLT -> +5V
- R8 pad 2: ARDUINO-A4 -> CLT
- R9 pad 1: IAT -> Net-(Q1-Pad2)
- R9 pad 2: ARDUINO-A5 -> ARDUINO-D38
- U1 pad 1: Net-(C2-Pad1) -> +12V
- U1 pad 2: Net-(C2-Pad2) -> GND
- U2 pad 1: +5V -> Net-(D1-Pad1)
- U2 pad 2: ATTINY-D10 -> GND
- U2 pad 3: ARDUINO-RST -> +5V
- U3 pad 1: Vehicle Down -> Net-(C6-Pad1)
- U3 pad 10: (no net) -> +5V
- U3 pad 2: ATTINY-A2 -> Net-(C6-Pad2)
- U3 pad 3: NEUTRAL SW -> unconnected-(U3-Pad3)
- U3 pad 4: ATTINY-A3 -> GND
- U3 pad 5: KICKSTAND SW -> GND
- U3 pad 6: ATTINY-A4 -> GND
- U3 pad 7: GND -> ARDUINO-D19
- U3 pad 8: (no net) -> unconnected-(U3-Pad8)
- U3 pad 9: (no net) -> GND
- U4 pad 2: Net-(R24-Pad2) -> ATTINY-D10
- U4 pad 3: unconnected-(U4-Pad3) -> ARDUINO-RST
- U4 pad 4: GND -> +5V
- U4 pad 5: GND -> ARDUINO-D32
- U4 pad 6: Net-(R32-Pad1) -> unconnected-(U4-Pad6)
- U4 pad 7: Net-(R32-Pad1) -> Net-(A1-Pad16)
- U4 pad 8: +5V -> Net-(A1-Pad15)
- U5 pad 1: +12V -> Vehicle Down
- U5 pad 2: GND -> ATTINY-A2
- U6 pad 1: Net-(D3-Pad1) -> +5V
- U6 pad 2: GND -> Net-(R12-Pad2)
- U6 pad 3: +5V -> unconnected-(U6-Pad3)
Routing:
- net GND: track 680.1 -> 231.6 mm, vias 14 -> 0
- net +5V: track 429.0 -> 107.2 mm, vias 3 -> 4
- net CLT: track 161.9 -> 15.0 mm
- net O2S +: track 146.5 -> 12.5 mm
- net MAP: track 142.1 -> 12.0 mm
- net +12V: track 157.3 -> 27.4 mm
- net CKP -: track 132.0 -> 6.58 mm, vias 3 -> 0
- net ARDUINO-D3: track 123.2 -> 0.00 mm, vias 2 -> 0
- net TPS: track 134.2 -> 11.4 mm
- net SELF DIAG: track 0.00 -> 116.0 mm, vias 0 -> 2
- net IAT: track 135.0 -> 19.1 mm
- net FAN RELAY: track 143.2 -> 29.0 mm, vias 2 -> 0
- net +BATT: track 130.8 -> 18.1 mm, vias 2 -> 0
- net CKP +: track 116.7 -> 17.2 mm, vias 2 -> 0
- net TEMP WARN: track 132.9 -> 45.6 mm, vias 1 -> 0
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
